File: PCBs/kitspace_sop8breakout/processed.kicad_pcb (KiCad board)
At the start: 2 copper layers, 83.3 x 63.2 mm, 48 parts, among them IC1 MCP6002, IC10 MCP6002, IC11 MCP6002, IC12 MCP6002, IC13 MCP6002, IC14 MCP6002, IC15 MCP6002, IC16 MCP6002, IC2 MCP6002, IC3 MCP6002, IC4 MCP6002, IC5 MCP6002, IC6 MCP6002, IC7 MCP6002, IC8 MCP6002, IC9 MCP6002, P1 CONN_01X04, P10 CONN_01X04, P11 CONN_01X04, P12 CONN_01X04, P13 CONN_01X04, P14 CONN_01X04, P15 CONN_01X04, P16 CONN_01X04, P2 CONN_01X04, P3 CONN_01X04, P4 CONN_01X04, P5 CONN_01X04, P6 CONN_01X04, P7 CONN_01X04, P8 CONN_01X04, P9 CONN_01X04

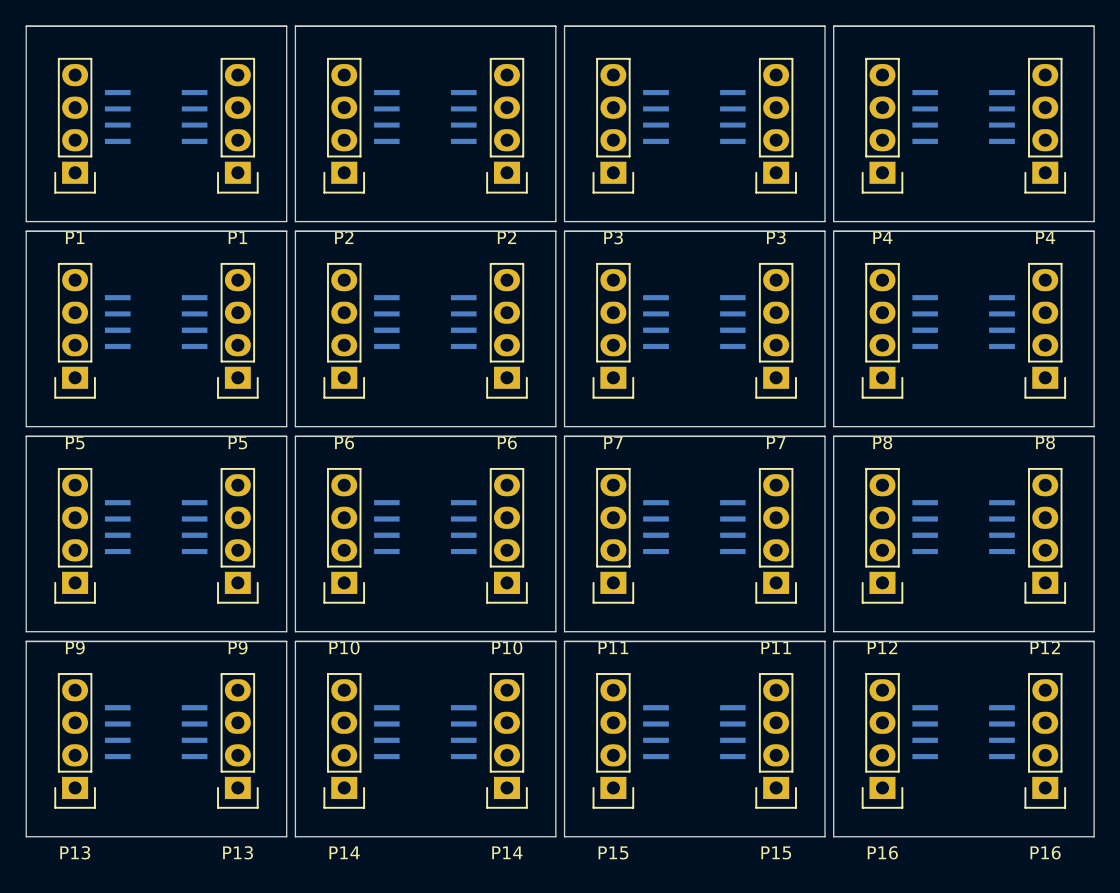
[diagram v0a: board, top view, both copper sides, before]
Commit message: recheck all circuits and clean up fill zone by rerouting the nets using freerouting and manually
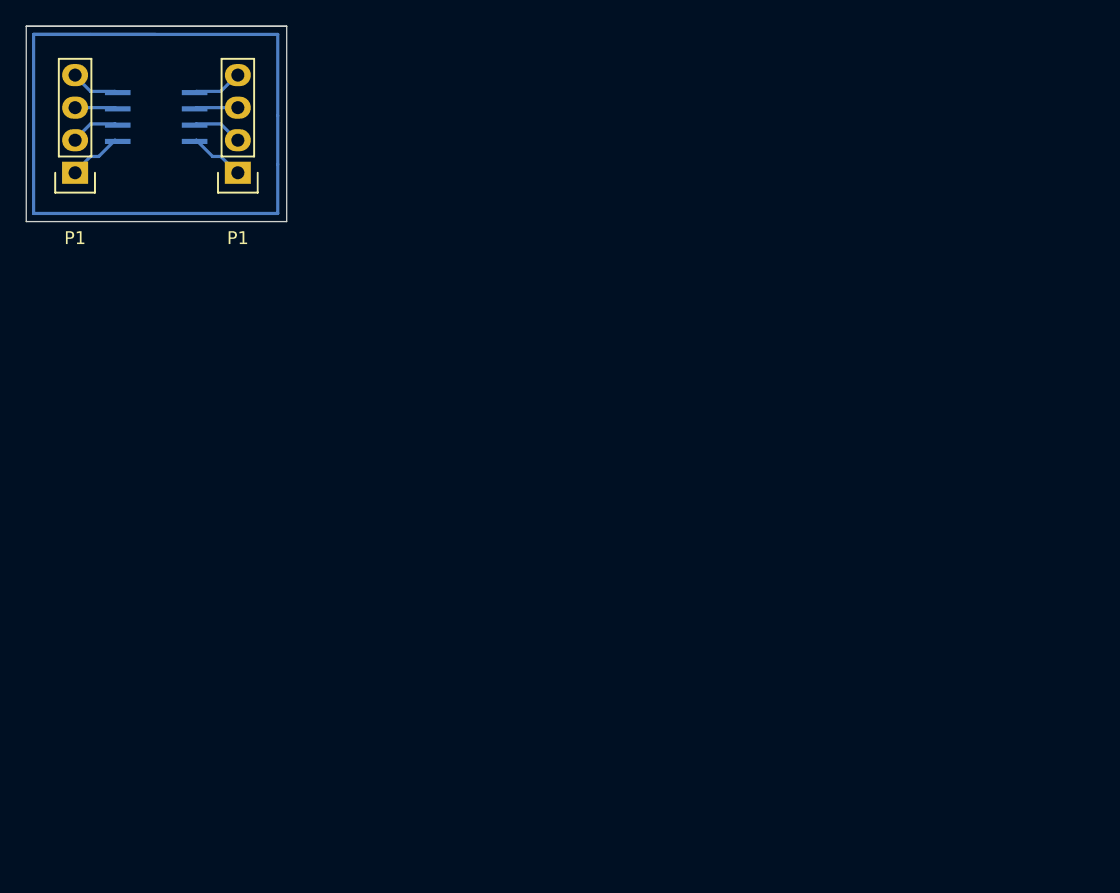
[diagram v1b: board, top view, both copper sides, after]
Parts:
- removed IC10, IC11, IC12, IC13, IC14, IC15, IC16, IC2, IC3, IC4, IC5, IC6, IC7, IC8, IC9: MCP6002, sop8:SOP-8
- removed P10 (x2), P11 (x2), P12 (x2), P13 (x2), P14 (x2), P15 (x2), P16 (x2), P2 (x2), P3 (x2), P4 (x2), P5 (x2), P6 (x2), P7 (x2), P8 (x2), P9 (x2): CONN_01X04, Pin_Headers:Pin_Header_Straight_1x04
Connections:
- IC1 pad 1: (no net) -> Net-(IC1-Pad1)
- IC1 pad 2: (no net) -> Net-(IC1-Pad2)
- IC1 pad 3: (no net) -> Net-(IC1-Pad3)
- IC1 pad 4: (no net) -> Net-(IC1-Pad4)
- IC1 pad 5: (no net) -> Net-(IC1-Pad5)
- IC1 pad 6: (no net) -> Net-(IC1-Pad6)
- IC1 pad 7: (no net) -> Net-(IC1-Pad7)
- IC1 pad 8: (no net) -> Net-(IC1-Pad8)
- P1 pad 1: (no net) -> Net-(IC1-Pad1)
- P1 pad 2: (no net) -> Net-(IC1-Pad2)
- P1 pad 3: (no net) -> Net-(IC1-Pad3)
- P1 pad 4: (no net) -> Net-(IC1-Pad4)
- P1 pad 1: (no net) -> Net-(IC1-Pad8)
- P1 pad 2: (no net) -> Net-(IC1-Pad7)
- P1 pad 3: (no net) -> Net-(IC1-Pad6)
- P1 pad 4: (no net) -> Net-(IC1-Pad5)
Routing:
- net (no net): track 0.00 -> 75.6 mm
- net Net-(IC1-Pad1): track 0.00 -> 4.53 mm
- net Net-(IC1-Pad8): track 0.00 -> 4.46 mm
- net Net-(IC1-Pad4): track 0.00 -> 4.00 mm
- net Net-(IC1-Pad2): track 0.00 -> 4.00 mm
- net Net-(IC1-Pad7): track 0.00 -> 3.93 mm
- net Net-(IC1-Pad5): track 0.00 -> 3.93 mm
- net Net-(IC1-Pad6): track 0.00 -> 3.40 mm
- net Net-(IC1-Pad3): track 0.00 -> 3.35 mm
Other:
- board size 83.3 x 63.2 mm -> 20.3 x 15.2 mm

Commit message: clean psbc that are missed before
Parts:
- renumbered P1 to P1_2

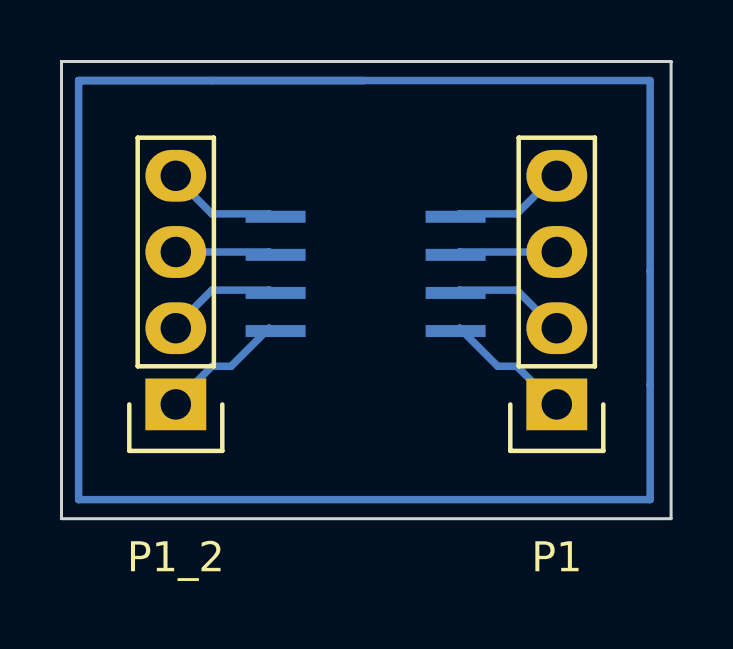
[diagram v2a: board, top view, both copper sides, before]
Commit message: delete unuseful wires of a PCB
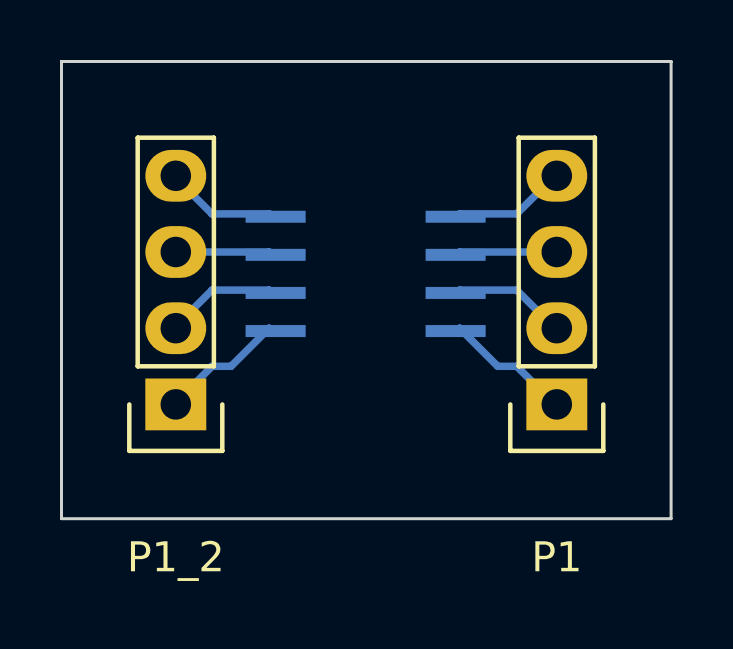
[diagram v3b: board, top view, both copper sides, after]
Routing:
- net (no net): track 75.6 -> 0.00 mm
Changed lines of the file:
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@@
     (width 0.1))
-  (segment
-    (start 139.065 98.425)
-    (end 158.115 98.425)
-    (width 0.25)
-    (layer B.Cu)
-    (net 0))
-  (segment
-    (start 158.115 98.425)
-    (end 158.115 104.775)
-    (width 0.25)
-    (layer B.Cu)
-    (net 0))
-  (segment
-    (start 158.115 104.775)
-    (end 158.115 108.573102)
-    (width 0.25)
-    (layer B.Cu)
-    (net 0))
-  (segment
-    (start 158.115 108.573102)
-    (end 158.115 112.395)
-    (width 0.25)
-    (layer B.Cu)
-    (net 0))
-  (segment
-    (start 158.115 112.395)
-    (end 139.065 112.395)
-    (width 0.25)
-    (layer B.Cu)
-    (net 0))
-  (segment
-    (start 139.065 112.395)
-    (end 139.065 98.425)
-    (width 0.25)
-    (layer B.Cu)
-    (net 0))
-  (segment
-    (start 139.065 98.425)
-    (end 143.51 98.425)
-    (width 0.25)
-    (layer B.Cu)
-    (net 0))
-  (segment
-    (start 143.51 98.425)
-    (end 148.59 98.425)
-    (width 0.25)
-    (layer B.Cu)
-    (net 0))
   (segment
     (start 145.415 106.68)
